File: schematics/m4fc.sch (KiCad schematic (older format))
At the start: 37 parts

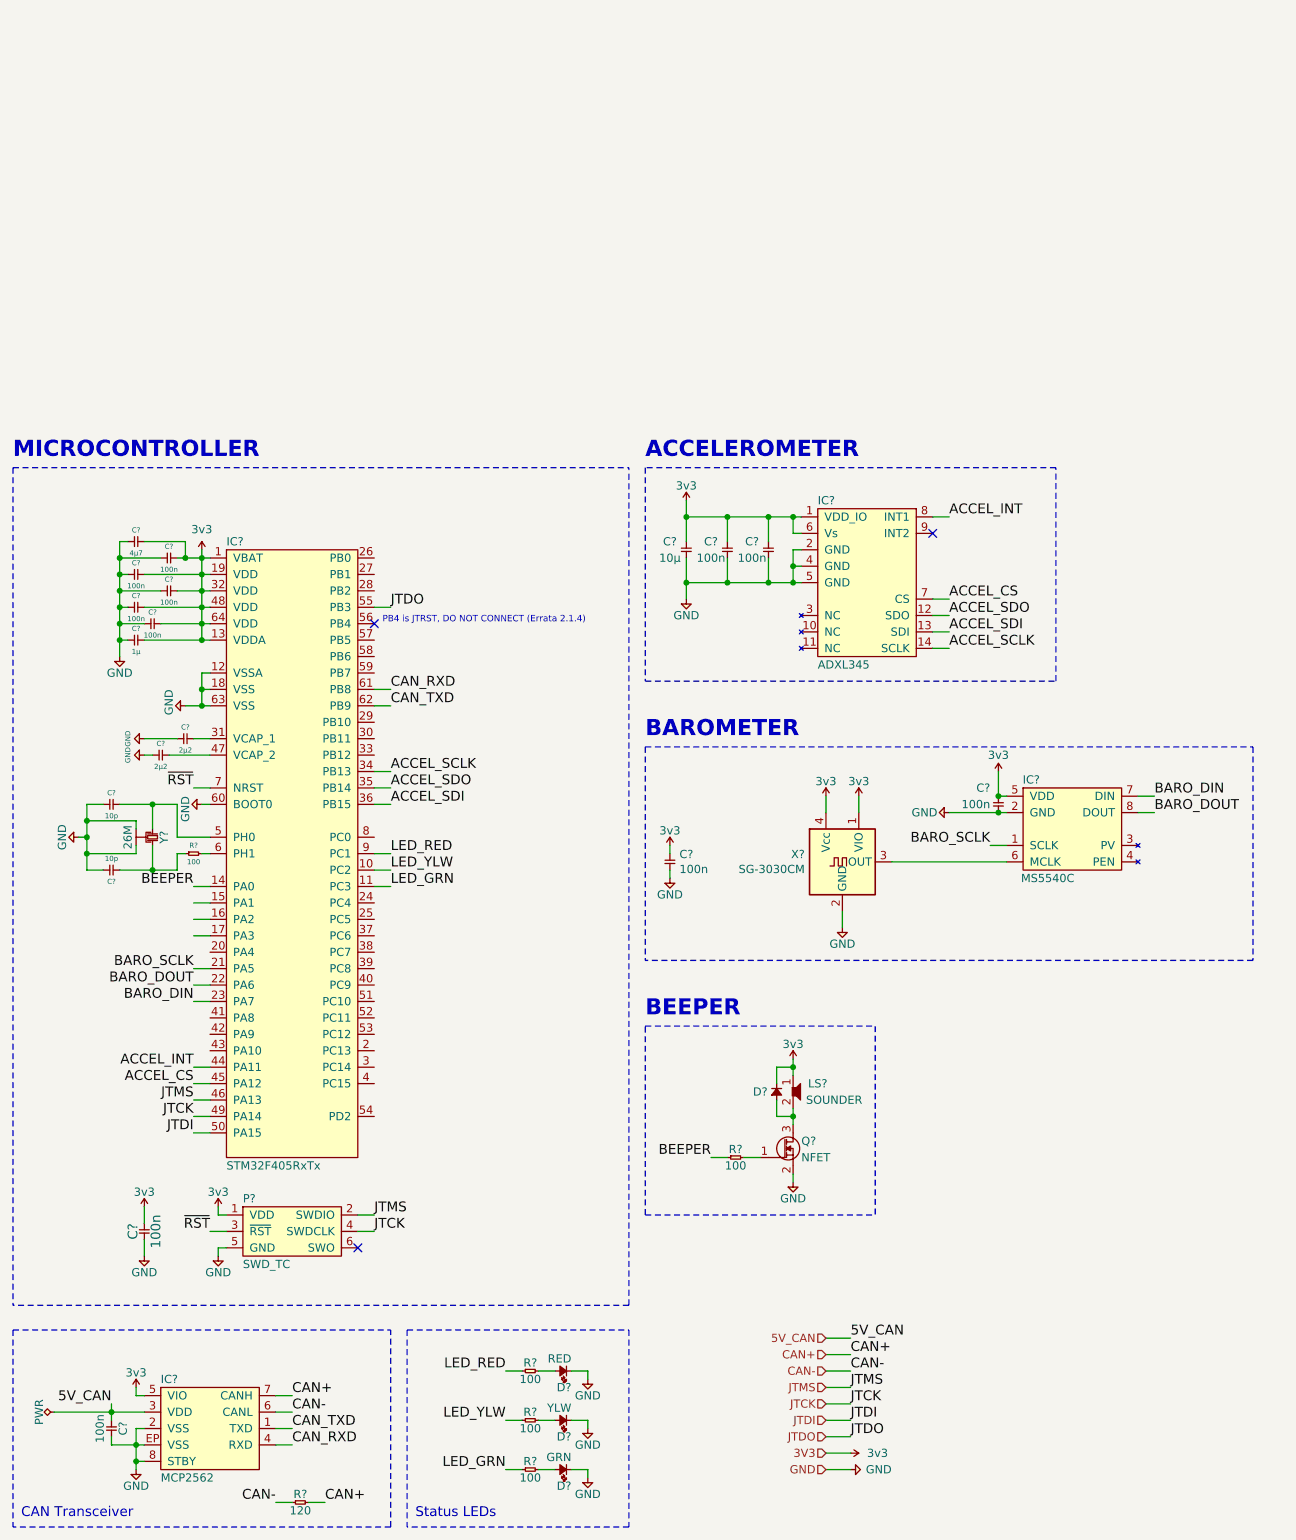
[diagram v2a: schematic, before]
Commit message: Master layout reorganisation and cleanup
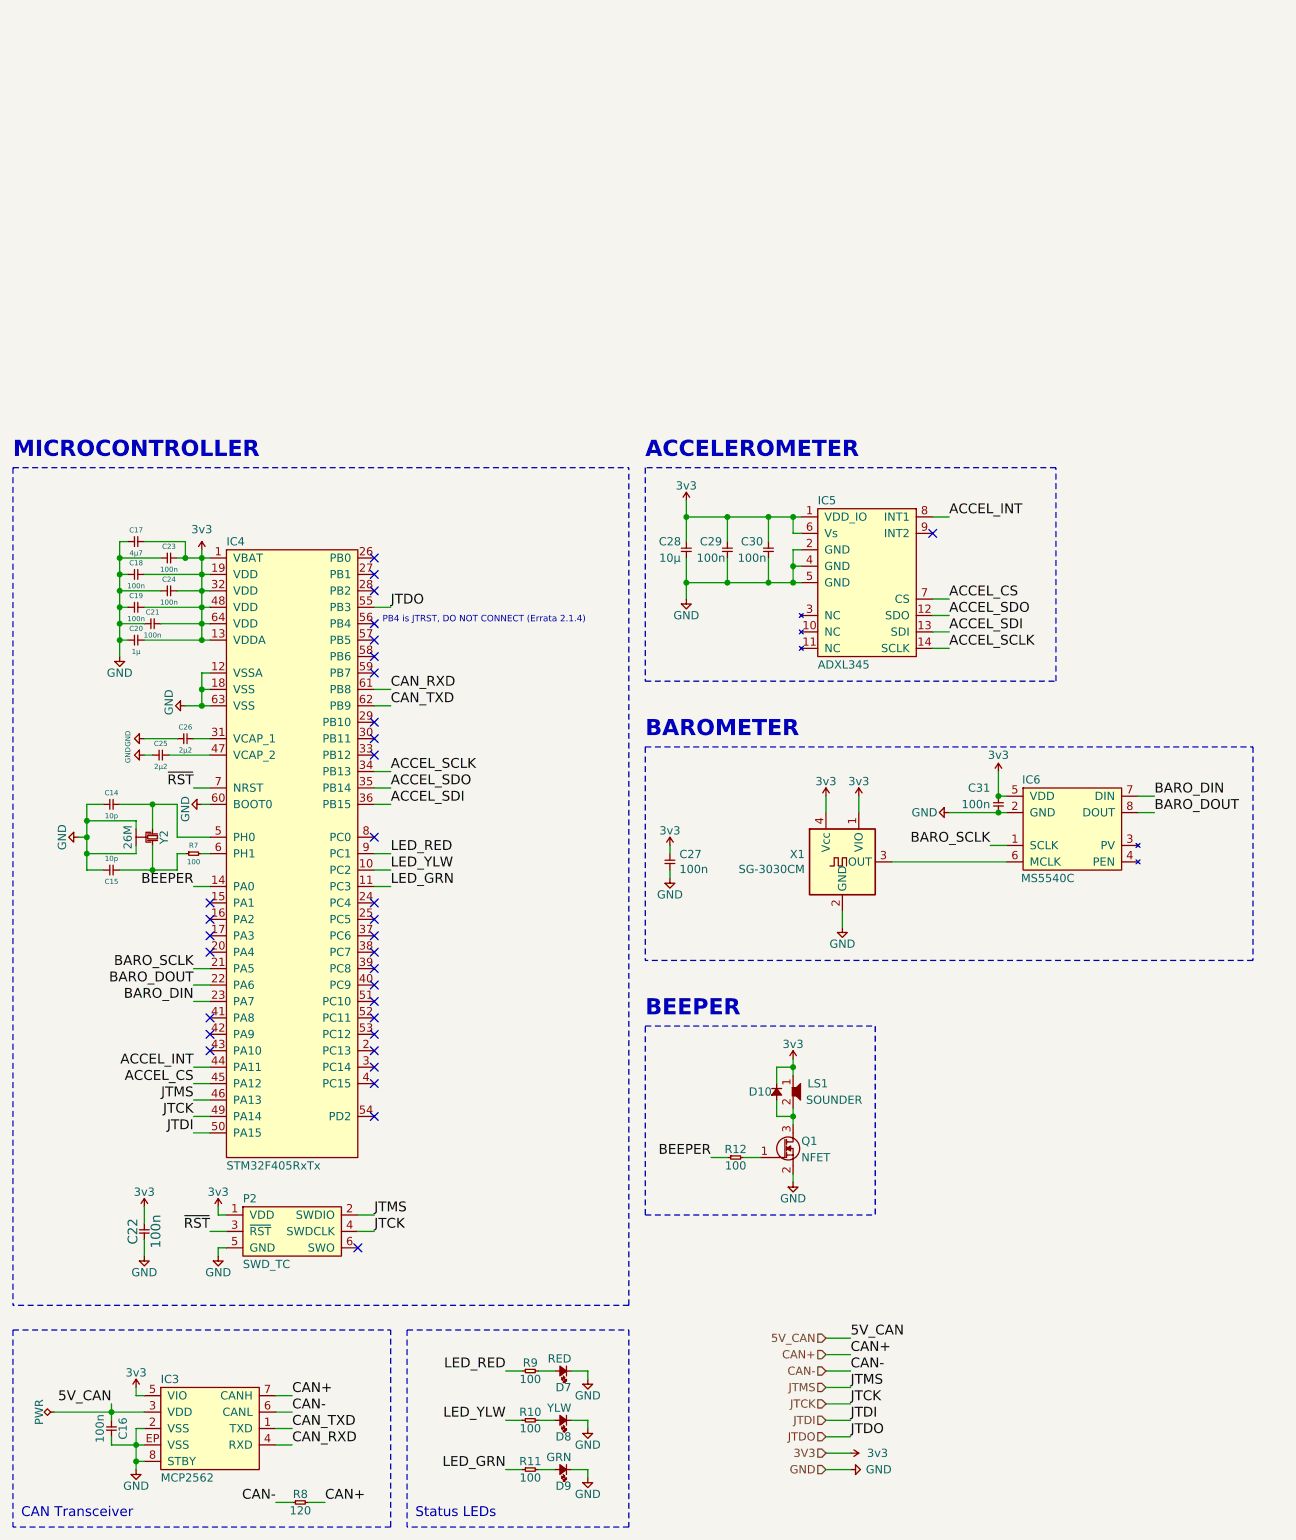
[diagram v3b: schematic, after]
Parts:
- removed C? (x5): 100n, agg:0402, symbol cusf-kicad:C
- removed C?: 1µ, agg:0402, symbol cusf-kicad:C
- removed C?: 4µ7, agg:0402, symbol cusf-kicad:C
- removed D?: RED, agg:0603-LED, symbol cusf-kicad:LED
- removed D?: YLW, agg:0603-LED, symbol cusf-kicad:LED
- removed IC?: MCP2562, agg:DFN-8-EP-MICROCHIP, symbol cusf-kicad:MCP2562
- removed P?: SWD_TC, agg:TC2030-NL, symbol cusf-kicad:SWD_TC
- removed R?: 120, agg:0603, symbol cusf-kicad:R
- removed R? (x3): 100, agg:0402, symbol cusf-kicad:R
- added C17: 4µ7, agg:0402, symbol cusf-kicad:C
- added C18, C19, C21, C23, C24: 100n, agg:0402, symbol cusf-kicad:C
- added C20: 1µ, agg:0402, symbol cusf-kicad:C
- added D7: RED, agg:0603-LED, symbol cusf-kicad:LED
- added D8: YLW, agg:0603-LED, symbol cusf-kicad:LED
- added IC3: MCP2562, agg:DFN-8-EP-MICROCHIP, symbol cusf-kicad:MCP2562
- added P2: SWD_TC, agg:TC2030-NL, symbol cusf-kicad:SWD_TC
- added R10, R11, R9: 100, agg:0402, symbol cusf-kicad:R
- added R8: 120, agg:0603, symbol cusf-kicad:R
- gave numbers to parts that had none: 22
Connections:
- net 3v3: now also C17.2, C18.2, C19.2, C20.2, C21.2, C23.2, C24.2, IC3.5 (VIO), P2.1 (VDD)
- net 5V_CAN: now also IC3.3 (VDD)
- net CAN+: now also IC3.7 (CANH), R8.2
- net CAN-: now also IC3.6 (CANL), R8.1
- net CAN_RXD: now also IC3.4 (RXD)
- net CAN_TXD: now also IC3.1 (TXD)
- net GND: now also C17.1, C18.1, C19.1, C20.1, C21.1, C23.1, C24.1, D7.1, D8.1, IC3.2 (VSS), IC3.8 (STBY), IC3.EP (VSS), P2.5 (GND)
- net JTCK: now also P2.4 (SWDCLK)
- net JTMS: now also P2.2 (SWDIO)
- net LED_GRN: now also R11.1
- net LED_RED: now also R9.1
- net LED_YLW: now also R10.1
- net ~RST: now also P2.3 (~RST)
- net at D9.2: now also R11.2
- new net: D7.2, R9.2
- new net: D8.2, R10.2
- no-connect marks 3 -> 33

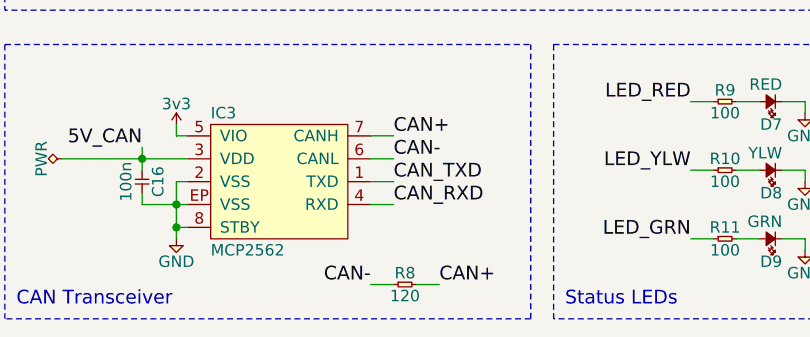
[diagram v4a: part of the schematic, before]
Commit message: Restructure main schematic bus layout
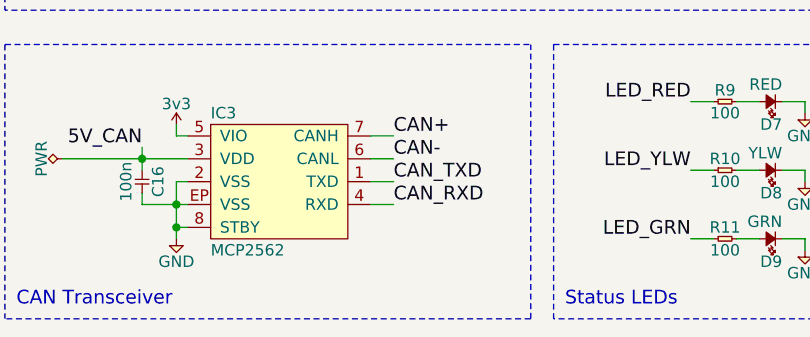
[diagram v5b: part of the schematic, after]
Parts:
- removed R8: 120, agg:0603, symbol cusf-kicad:R
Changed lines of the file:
@@
 Wire Wire Line
 	2800 5850 2900 5850
-$Comp
-L cusf-kicad:R R8
-U 1 1 60BFC5F7
-P 2300 9600
-F 0 "R8" H 2350 9650 50  0000 C CNN
-F 1 "120" H 2350 9550 50  0000 C CNN
-F 2 "agg:0603" H 2300 9600 50  0001 C CNN
-F 3 "" H 2300 9600 50  0001 C CNN
-F 4 "9238379" H 2300 9600 60  0001 C CNN "Farnell"
-	1    2300 9600
-	1    0    0    -1
-$EndComp
-Text Label 2200 9600 2    60   ~ 0
-CAN-
-Wire Wire Line
-	2200 9600 2300 9600
-Text Label 2500 9600 0    60   ~ 0
-CAN+
-Wire Wire Line
-	2500 9600 2400 9600
 NoConn ~ 2800 4250
 $Comp

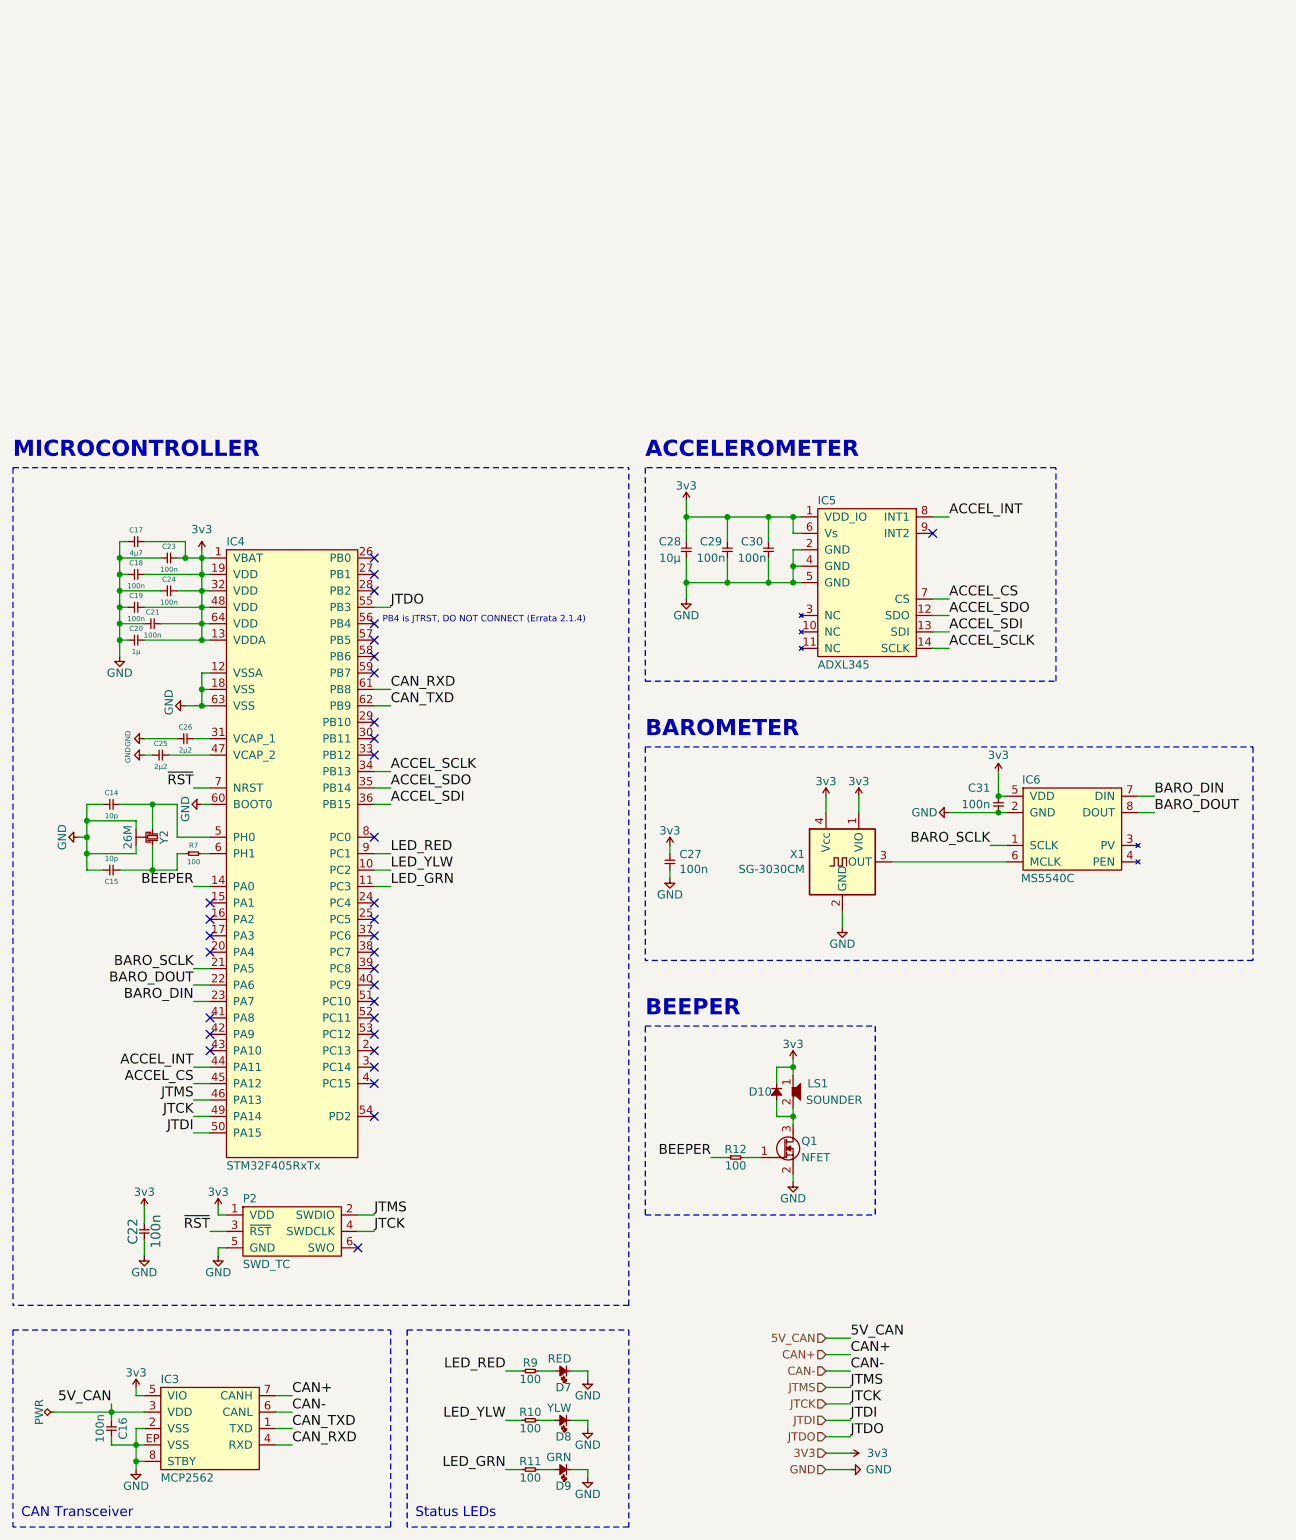
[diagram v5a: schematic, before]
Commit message: Normalise all font sizes to 50 mil
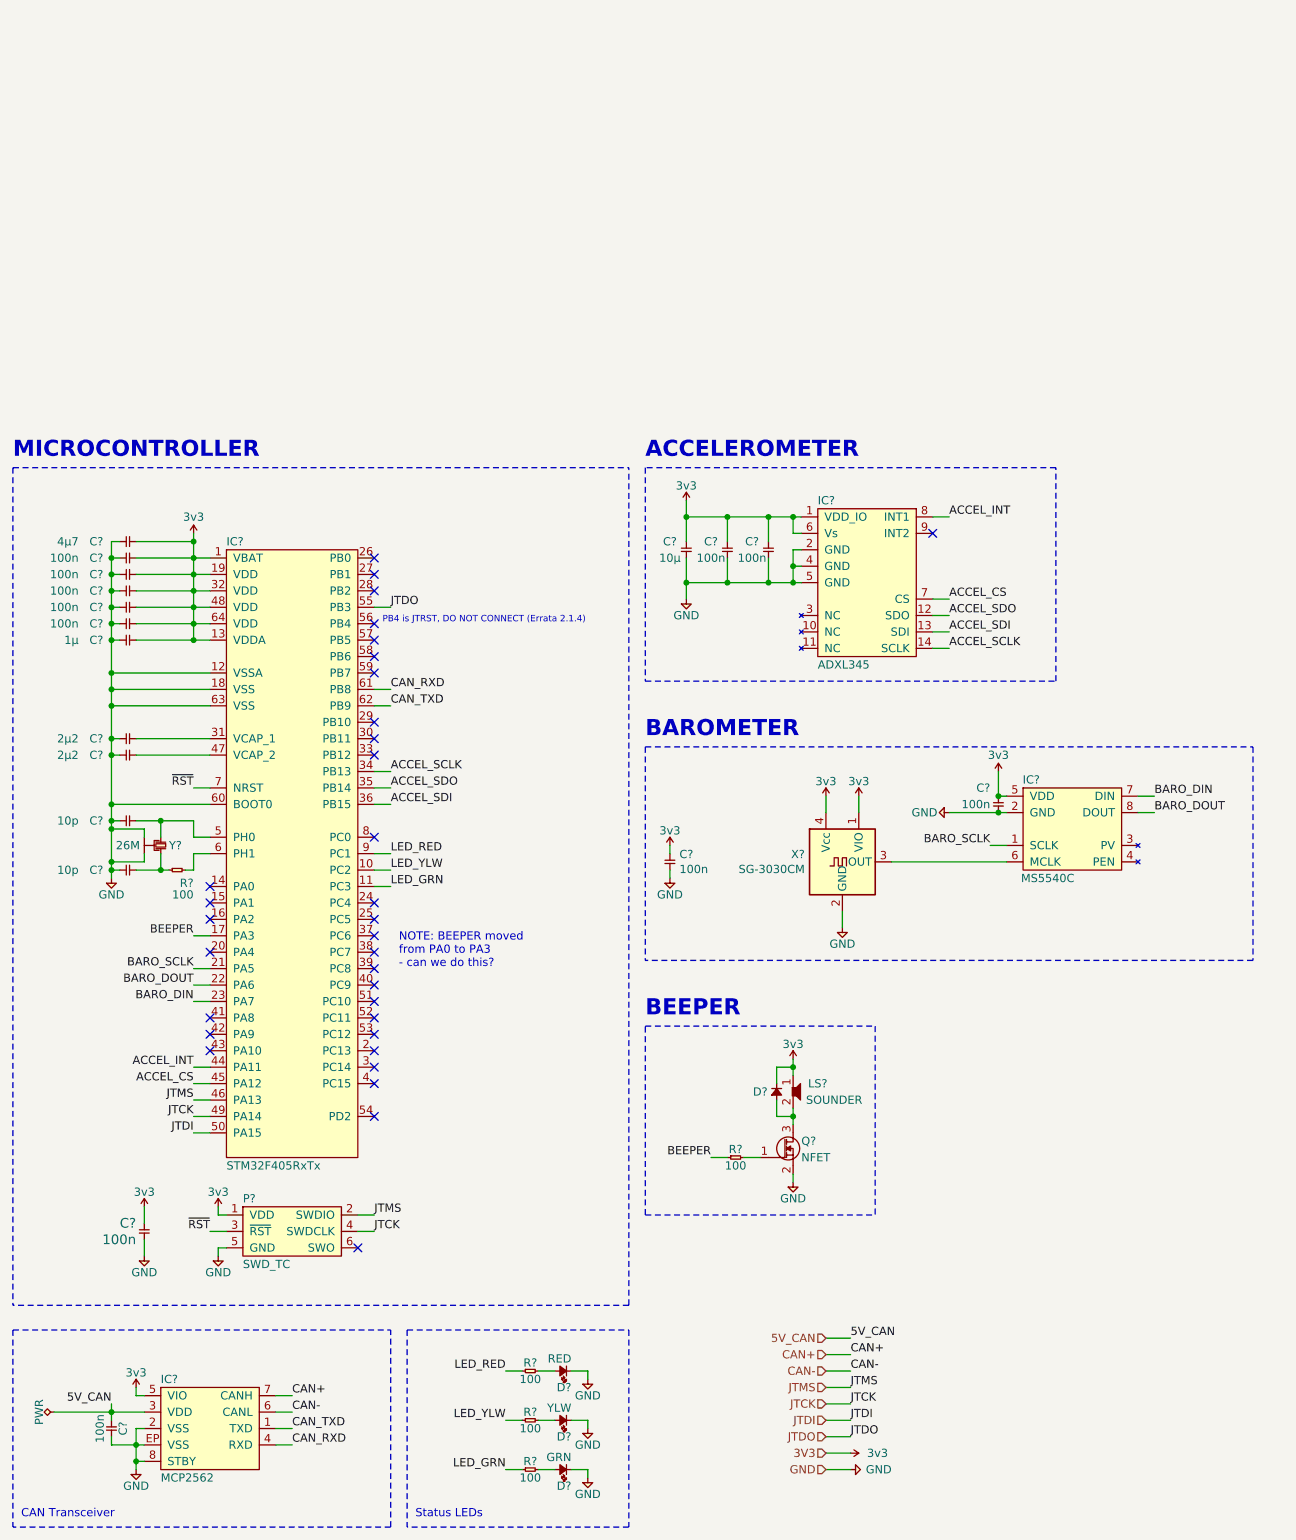
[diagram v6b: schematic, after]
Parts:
- removed C14, C15: 10p, agg:0402, symbol cusf-kicad:C
- removed C17: 4µ7, agg:0402, symbol cusf-kicad:C
- removed C18, C19, C21, C23, C24: 100n, agg:0402, symbol cusf-kicad:C
- removed C20: 1µ, agg:0402, symbol cusf-kicad:C
- removed C25, C26: 2µ2, agg:0402, symbol cusf-kicad:C
- removed R7: 100, agg:0402, symbol cusf-kicad:R
- removed Y2: 26M, agg:XTAL-20x16, symbol cusf-kicad:SMD_XTAL
- added C? (x2): 2µ2, agg:0402, symbol cusf-kicad:C
- added C? (x5): 100n, agg:0402, symbol cusf-kicad:C
- added C?: 1µ, agg:0402, symbol cusf-kicad:C
- added C?: 4µ7, agg:0402, symbol cusf-kicad:C
- added C? (x2): 10p, agg:0402, symbol cusf-kicad:C
- added R?: 100, agg:0402, symbol cusf-kicad:R
- added Y?: 26M, agg:XTAL-20x16, symbol cusf-kicad:SMD_XTAL
- renumbered C29 to C?, C28 to C?, C30 to C?, C16 to C?, C22 to C?, C31 to C?, C27 to C?, D10 to D?, D9 to D?, D7 to D?, D8 to D?, IC5 to IC?, IC4 to IC?, IC6 to IC?, IC3 to IC?, LS1 to LS?, P2 to P?, Q1 to Q?, R12 to R?, R9 to R?, R10 to R?, R11 to R?, X1 to X?
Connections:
- net 3v3: now also C?.2, C?.2, C?.2, C?.2, C?.2, C?.2, C?.2
- net BEEPER: now also IC?.17 (PA3); no longer IC?.14 (PA0)
- net GND: now also C?.1, C?.1, C?.1, C?.1, C?.1, C?.1, C?.1, C?.1, C?.1, C?.1, C?.1, Y?.2, Y?.4
- net at IC?.31 (VCAP_1): now also C?.2
- net at IC?.47 (VCAP_2): now also C?.2
- net at IC?.5 (PH0): now also C?.2, Y?.1
- net at IC?.6 (PH1): now also R?.2
- new net: C?.2, R?.1, Y?.3
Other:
- note added: "NOTE: BEEPER moved\nfrom PA0 to PA3\n- can we do this?"
